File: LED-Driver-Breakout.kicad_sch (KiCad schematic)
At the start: 0 parts

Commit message: finished board - need review
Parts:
- added C1, C2: C, symbol Device:C
- added F1: Fuse, symbol Device:Fuse
- added PS1: LDH-45B-1050, LDH-45B-1050:CONV_LDH-45B-1050, symbol LDH-45B-1050:LDH-45B-1050
- added U1: V10P45-M3/86A, SOT_45-M3/86A_VIS, symbol 2026-02-02_22-16-14:V10P45-M3_86A
- added U2: TSR0.5-2418, Converter_DCDC:Converter_DCDC_TRACO_TSR0.5-24xx_TSR0.5-24xxx_THT, symbol Converter_DCDC:TSR0.5-2418
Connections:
- new net: F1.2, U1.1 (ANODE), U1.2 (ANODE)
- new net +BATT: F1.1
- new net GND: C1.2, C2.2, PS1.2 (VIN-), U2.2 (GND)
- new net VOUT+: PS1.7 (VOUT+)
- new net VOUT-: PS1.6 (VOUT-)
- new net VRegulated: U2.3 (Vout)
- new net V_Fused: C1.1, C2.1, PS1.1 (VIN+), U1.3 (CATHODE), U2.1 (Vin)

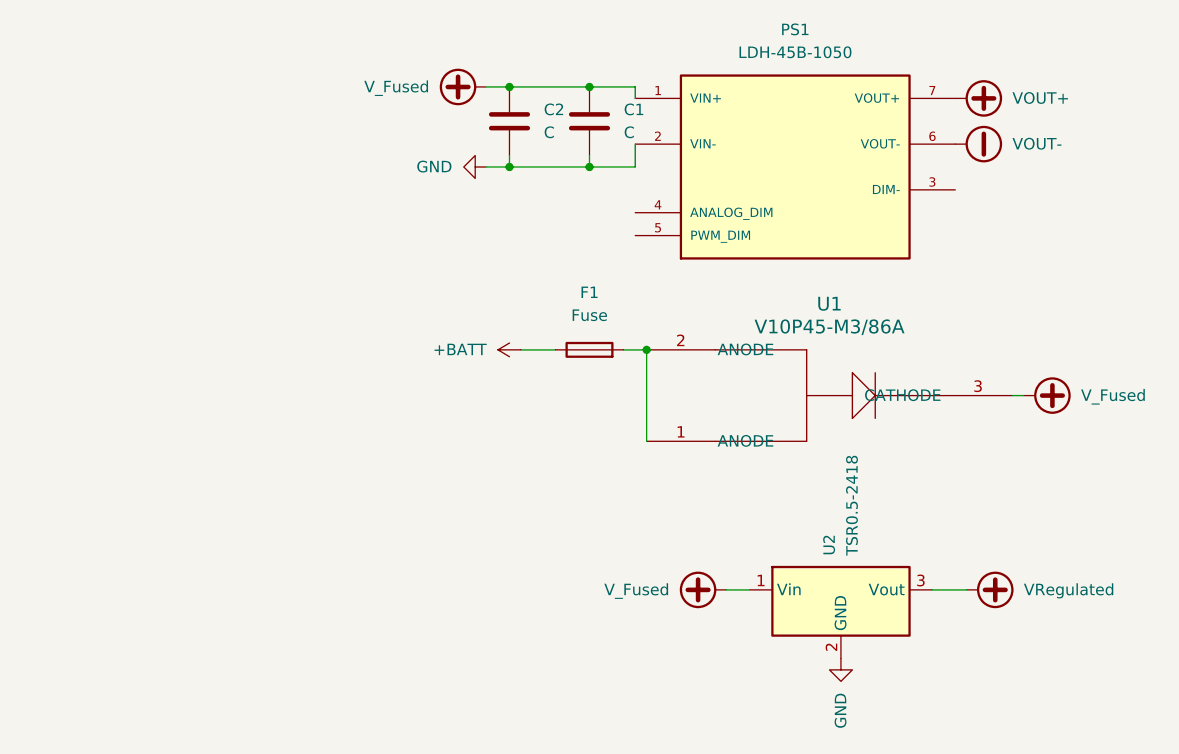
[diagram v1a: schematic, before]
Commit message: finished pcb routing may need to make the board more square
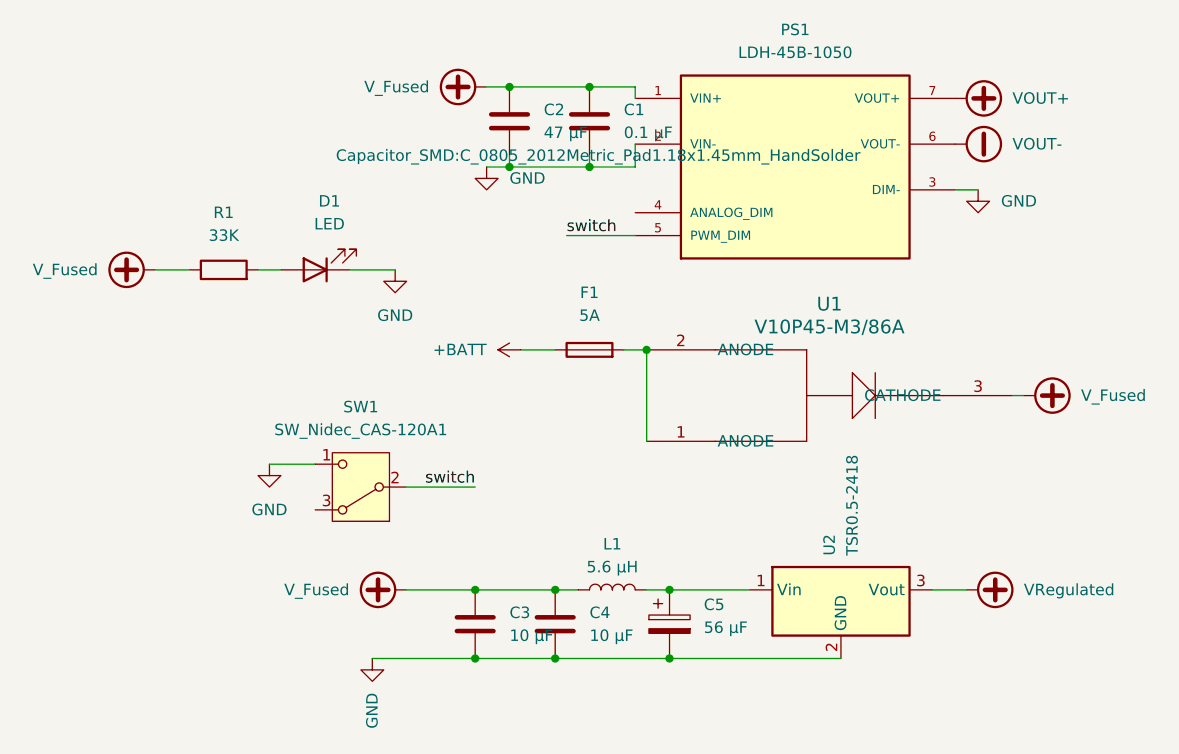
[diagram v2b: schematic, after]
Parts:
- added C3, C4: 10 µF, Capacitor_SMD:C_0805_2012Metric_Pad1.18x1.45mm_HandSolder, symbol Device:C
- added C5: 56 µF, Capacitor_SMD:CP_Elec_8x10, symbol Device:C_Polarized
- added D1: LED, LED_SMD:LED_1206_3216Metric_Pad1.42x1.75mm_HandSolder, symbol Device:LED
- added L1: 5.6 µH, Inductor_SMD:L_0805_2012Metric_Pad1.05x1.20mm_HandSolder, symbol Device:L
- added R1: 33K, Resistor_SMD:R_1206_3216Metric_Pad1.30x1.75mm_HandSolder, symbol Device:R
- added SW1: SW_Nidec_CAS-120A1, Button_Switch_SMD:Nidec_Copal_CAS-120A, symbol Switch:SW_Nidec_CAS-120A1
- C1: value C -> 0.1 µF; footprint (none) -> Capacitor_SMD:C_0805_2012Metric_Pad1.18x1.45mm_HandSolder
- C2: value C -> 47 µF; footprint (none) -> Capacitor_SMD:C_Elec_6.3x7.7
- F1: value Fuse -> 5A; footprint (none) -> KiCad333:154005DR
- PS1: footprint LDH-45B-1050:CONV_LDH-45B-1050 -> KiCad:LDH45B1050
- U1: footprint SOT_45-M3/86A_VIS -> Diode_SMD:D_PowerDI-5
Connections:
- net GND: now also PS1.3 (DIM-), C3.2, C4.2, C5.2, D1.1 (K), SW1.1 (C)
- net V_Fused: now also C3.1, C4.1, L1.1, R1.1; no longer U2.1 (Vin)
- net switch: now reaches PS1.5 (PWM_DIM)
- net switch: now also SW1.2 (B)
- new net: D1.2 (A), R1.2
- new net: C5.1, L1.2, U2.1 (Vin)

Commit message: Updates to schematic.
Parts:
- C1: footprint Capacitor_SMD:C_0805_2012Metric_Pad1.18x1.45mm_HandSolder -> C
- U2: value TSR0.5-2418 -> TSR0.5-24120
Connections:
- no-connect marks 0 -> 2
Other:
- note added: "12VDC Switching Regulator"
- note added: "LED On/Off Switch"
- note added: "Main LED Driver"
- note added: "Power Indicator"
- note added: "Reverse Polarity Protection"
- moved on the sheet: C1, C2, C3, C4, C5, D1, F1, L1, PS1, R1, SW1, U1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

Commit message: Added project-specific libs/fps; updates generally; broken rn.
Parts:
- removed F1: 5A, KiCad333:154005DR, symbol Device:Fuse
- removed PS1: LDH-45B-1050, KiCad:LDH45B1050, symbol LDH-45B-1050:LDH-45B-1050
- removed U1: V10P45-M3/86A, Diode_SMD:D_PowerDI-5, symbol 2026-02-02_22-16-14:V10P45-M3_86A
- removed U2: TSR0.5-24120, Converter_DCDC:Converter_DCDC_TRACO_TSR0.5-24xx_TSR0.5-24xxx_THT, symbol Converter_DCDC:TSR0.5-2418
- added C6: 10 µF, Capacitor_SMD:C_0805_2012Metric_Pad1.18x1.45mm_HandSolder, symbol Device:C
- added F1: 5A, Project_Footprints_Lib:154005DR, symbol Project_Symbols_Lib:Fuse
- added J1: S2B-XH-A, Project_Footprints_Lib:JST_XH_S2B-XH-A_1x02_P2.50mm_Horizontal, symbol Project_Symbols_Lib:Connector-JST-RAngle-2pin
- added J2: LED Output, TerminalBlock_WAGO:TerminalBlock_WAGO_2601-3102_1x02_P3.50mm_Vertical, symbol Project_Symbols_Lib:Connector-WAGO-clamp-4pos
- added PS1: LDH-45B-1050, Project_Footprints_Lib:LDH-45B-1050, symbol Project_Symbols_Lib:LDH-45B-1050
- added U1: V10P45-M3/86A, Diode_SMD:D_PowerDI-5, symbol Project_Symbols_Lib:V10P45-M3_86A
- added U2: TSR2-24120, Converter_DCDC:Converter_DCDC_TRACO_TSR2-xxxx_THT, symbol Converter_DCDC:TSR2-24120
- C1: footprint C -> Project_Footprints_Lib:C_0805_2012Metric_Pad1.18x1.45mm_HandSolder
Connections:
- net GND: now also PS1.3 (DIM-); no longer C1.2, C2.2, C3.2, C4.2, C5.2
- net V_Fused: now also PS1.1 (VIN+), U1.1
- net switch: now also PS1.5 (PWM_DIM)
- net at C5.1, L1.2: now also C6.1, U2.1 (Vin)
- new net: J2.1, PS1.7 (VOUT+)
- new net: J2.2, PS1.6 (VOUT-)
- new net: C3.2, C4.2, C5.2, C6.2, J1.2, U2.2 (GND)
- new net: C1.2, C2.2, PS1.2 (VIN-)
- new net: F1.2, U1.2
- new net: J1.1, U2.3 (Vout)
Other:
- note added: "* Create a GND net for KiCad ERC."
- moved on the sheet: C3, C4, C5, L1

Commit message: Relayout in progress.
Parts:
- removed SW1: SW_Nidec_CAS-120A1, Button_Switch_SMD:Nidec_Copal_CAS-120A, symbol Switch:SW_Nidec_CAS-120A1
- added J3: XT60, Connector_AMASS:AMASS_XT60PW-M_1x02_P7.20mm_Horizontal, symbol Project_Symbols_Lib:Connector-XT60M
- added J4: 01x03_PinHeaderSwitch, Connector_PinHeader_2.54mm:PinHeader_1x03_P2.54mm_Vertical, symbol Connector:Conn_01x03_Pin
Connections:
- net GND: now also J3.1, J4.1 (Pin_1)
- net switch: now also J4.2 (Pin_2)
- net at F1.1: now also J3.2
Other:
- note added: "Reverse Polarity Protection/Battery Input"
- note removed: "Reverse Polarity Protection"
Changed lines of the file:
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@@
 		)
 	)
-	(text "Reverse Polarity Protection"
-		(exclude_from_sim no)
-		(at 49.53 109.22 0)
+	(text "Reverse Polarity Protection/Battery Input"
+		(exclude_from_sim no)
+		(at 55.372 109.982 0)
 		(effects
 			(font
@@
 	)
 	(no_connect
-		(at 43.18 156.21)
+		(at 73.66 78.74)
 	)
 	(no_connect
-		(at 73.66 78.74)
+		(at 49.53 154.94)
+	)
+	(wire
+		(pts
+			(xy 50.8 129.54) (xy 52.07 129.54)
+		)
+		(stroke
+			(width 0)
+			(type default)
+		)
 	)
 	(wire
@@
 	(wire
 		(pts
-			(xy 38.1 151.13) (xy 43.18 151.13)
-		)
-		(stroke
-			(width 0)
-			(type default)
-		)
-	)
-	(wire
-		(pts
 			(xy 109.22 66.04) (xy 110.49 66.04)
 		)
@@
 	(wire
 		(pts
+			(xy 49.53 149.86) (xy 52.07 149.86)
+		)
+		(stroke
+			(width 0)
+			(type default)
+		)
+	)
+	(wire
+		(pts
 			(xy 46.99 175.26) (xy 48.26 175.26)
 		)
@@
 	(wire
 		(pts
-			(xy 60.96 153.67) (xy 53.34 153.67)
-		)
-		(stroke
-			(width 0)
-			(type default)
-		)
-	)
-	(wire
-		(pts
-			(xy 52.07 127) (xy 54.61 127)
-		)
-		(stroke
-			(width 0)
-			(type default)
-		)
-	)
-	(wire
-		(pts
 			(xy 109.22 71.12) (xy 110.49 71.12)
 		)
@@
 		(pts
 			(xy 118.11 177.8) (xy 118.11 182.88)
+		)
+		(stroke
+			(width 0)
+			(type default)
+		)
+	)
+	(wire
+		(pts
+			(xy 49.53 152.4) (xy 52.07 152.4)
+		)
+		(stroke
+			(width 0)
+			(type default)
+		)
+	)
+	(wire
+		(pts
+			(xy 50.8 127) (xy 54.61 127)
 		)
 		(stroke
@@
 	)
 	(label "GND"
+		(at 52.07 129.54 0)
+		(effects
+			(font
+				(size 1.27 1.27)
+			)
+			(justify left bottom)
+		)
+	)
+	(label "GND"
 		(at 111.76 76.2 0)
 		(effects
@@
 	)
 	(label "GND"
-		(at 38.1 151.13 180)
+		(at 52.07 149.86 0)
 		(effects
 			(font
 				(size 1.27 1.27)
 			)
-			(justify right bottom)
+			(justify left bottom)
 		)
 	)
@@
 	)
 	(label "switch"
-		(at 60.96 153.67 180)
+		(at 52.07 152.4 0)
 		(effects
 			(font
 				(size 1.27 1.27)
 			)
-			(justify right bottom)
+			(justify left bottom)
 		)
 	)
@@
 	)
 	(symbol
-		(lib_id "Switch:SW_Nidec_CAS-120A1")
-		(at 48.26 153.67 180)
-		(unit 1)
-		(exclude_from_sim no)
-		(in_bom yes)
-		(on_board no)
-		(dnp no)
-		(fields_autoplaced yes)
-		(property "Reference" "SW1"
-			(at 48.26 144.78 0)
-			(effects
-				(font
-					(size 1.27 1.27)
-				)
-			)
-		)
-		(property "Value" "SW_Nidec_CAS-120A1"
-			(at 48.26 147.32 0)
-			(effects
-				(font
-					(size 1.27 1.27)
-				)
-			)
-		)
-		(property "Footprint" "Button_Switch_SMD:Nidec_Copal_CAS-120A"
-			(at 48.26 143.51 0)
-			(effects
-				(font
-					(size 1.27 1.27)
-				)
-				(hide yes)
-			)
-		)
-		(property "Datasheet" "https://www.nidec-components.com/e/catalog/switch/cas.pdf"
-			(at 48.26 146.05 0)
-			(effects
-				(font
-					(size 1.27 1.27)
-				)
-				(hide yes)
-			)
-		)
-		(property "Description" "Switch, single pole double throw"
-			(at 48.26 153.67 0)
-			(effects
-				(font
-					(size 1.27 1.27)
-				)
-				(hide yes)
-			)
-		)
-		(pin "1"
-		)
-		(pin "3"
-		)
-		(pin "2"
-		)
-		(instances
-			(project ""
-				(path "/489043bf-45bc-433c-85b5-ac7612966c0c"
-					(reference "SW1")
-					(unit 1)
-				)
-			)
-		)
-	)
-	(symbol
 		(lib_id "Device:C")
 		(at 48.26 179.07 0)
@@
 	)
 	(symbol
+		(lib_id "Connector:Conn_01x03_Pin")
+		(at 44.45 152.4 0)
+		(unit 1)
+		(exclude_from_sim no)
+		(in_bom yes)
+		(on_board yes)
+		(dnp no)
+		(property "Reference" "J4"
+			(at 44.958 146.05 0)
+			(effects
+				(font
+					(size 1.27 1.27)
+				)
+			)
+		)
+		(property "Value" "01x03_PinHeaderSwitch"
+			(at 45.085 147.32 0)
+			(effects
+				(font
+					(size 1.27 1.27)
+				)
+				(hide yes)
+			)
+		)
+		(property "Footprint" "Connector_PinHeader_2.54mm:PinHeader_1x03_P2.54mm_Vertical"
+			(at 44.45 152.4 0)
+			(effects
+				(font
+					(size 1.27 1.27)
+				)
+				(hide yes)
+			)
+		)
+		(property "Datasheet" "~"
+			(at 44.45 152.4 0)
+			(effects
+				(font
+					(size 1.27 1.27)
+				)
+				(hide yes)
+			)
+		)
+		(property "Description" "Generic connector, single row, 01x03, script generated"
+			(at 44.45 152.4 0)
+			(effects
+				(font
+					(size 1.27 1.27)
+				)
+				(hide yes)
+			)
+		)
+		(pin "3"
+		)
+		(pin "1"
+		)
+		(pin "2"
+		)
+		(instances
+			(project ""
+				(path "/489043bf-45bc-433c-85b5-ac7612966c0c"
+					(reference "J4")
+					(unit 1)
+				)
+			)
+		)
+	)
+	(symbol
 		(lib_id "Project_Symbols_Lib:LDH-45B-1050")
 		(at 91.44 73.66 0)
@@
 	)
 	(symbol
-		(lib_id "power:+BATT")
-		(at 52.07 127 90)
-		(unit 1)
-		(exclude_from_sim no)
-		(in_bom yes)
-		(on_board yes)
-		(dnp no)
-		(fields_autoplaced yes)
-		(property "Reference" "#PWR07"
-			(at 55.88 127 0)
-			(effects
-				(font
-					(size 1.27 1.27)
-				)
-				(hide yes)
-			)
-		)
-		(property "Value" "+BATT"
-			(at 48.26 126.9999 90)
-			(effects
-				(font
-					(size 1.27 1.27)
-				)
-				(justify left)
-			)
-		)
-		(property "Footprint" ""
-			(at 52.07 127 0)
-			(effects
-				(font
-					(size 1.27 1.27)
-				)
-				(hide yes)
-			)
-		)
-		(property "Datasheet" ""
-			(at 52.07 127 0)
-			(effects
-				(font
-					(size 1.27 1.27)
-				)
-				(hide yes)
-			)
-		)
-		(property "Description" "Power symbol creates a global label with name \"+BATT\""
-			(at 52.07 127 0)
-			(effects
-				(font
-					(size 1.27 1.27)
-				)
-				(hide yes)
-			)
-		)
-		(pin "1"
-		)
-		(instances
-			(project ""
-				(path "/489043bf-45bc-433c-85b5-ac7612966c0c"
-					(reference "#PWR07")
-					(unit 1)
-				)
-			)
-		)
-	)
-	(symbol
 		(lib_id "Device:C_Polarized")
 		(at 87.63 179.07 0)
@@
 					(unit 1)
 				)
+			)
+		)
+	)
+	(symbol
+		(lib_id "Project_Symbols_Lib:Connector-XT60M")
+		(at 48.26 128.27 180)
+		(unit 1)
+		(exclude_from_sim no)
+		(in_bom yes)
+		(on_board yes)
+		(dnp no)
+		(fields_autoplaced yes)
+		(property "Reference" "J3"
+			(at 46.99 120.65 0)
+			(effects
+				(font
+					(size 1.27 1.27)
+				)
+			)
+		)
+		(property "Value" "XT60"
+			(at 46.99 123.19 0)
+			(effects
+				(font
+					(size 1.27 1.27)
+				)
+			)
+		)
+		(property "Footprint" "Connector_AMASS:AMASS_XT60PW-M_1x02_P7.20mm_Horizontal"
+			(at 48.26 128.27 0)
+			(effects
+				(font
+					(size 1.27 1.27)
+				)
+				(hide yes)
+			)
+		)
+		(property "Datasheet" "https://www.tme.com/Document/b13629717d44ae038681dba08d18c0b6/XT60PW-M.pdf"
+			(at 48.26 128.27 0)
+			(effects
+				(font
+					(size 1.27 1.27)
+				)
+				(hide yes)
+			)
+		)
+		(property "Description" "JST, 2-pin THT connector."
+			(at 48.26 128.27 0)
+			(effects
+				(font
+					(size 1.27 1.27)
+				)
+				(hide yes)
+			)
+		)
+		(pin "2"
+		)
+		(pin "1"
+		)
+		(instances
+			(project ""
+				(path "/489043bf-45bc-433c-85b5-ac7612966c0c"
+					(reference "J3")
+					(unit 1)
+				)

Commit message: did layout, still need to fix ERC errors and DRC warnings
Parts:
- added DRIVER_V_IN1, GND1, REGULATOR_IN1, SWITCH1, V_FUSED1, V_REGULATED1: TestPoint, TestPoint:TestPoint_Loop_D2.54mm_Drill1.5mm_Beaded, symbol Connector:TestPoint
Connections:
- net REGULATOR_V_IN: now reaches C5.1, C6.1, L1.2, U2.1 (Vin)
- net REGULATOR_V_IN: now also REGULATOR_IN1.1
- net V_REGULATED: now reaches J1.1, U2.3 (Vout)
- net V_REGULATED: now also V_REGULATED1.1
- removed net GND: D1.1 (K), J3.1, J4.1 (Pin_1), PS1.3 (DIM-)
- net V_Fused renamed +24V
- net +24V: now also DRIVER_V_IN1.1, V_FUSED1.1
- net switch renamed SWITCH
- net SWITCH: now also SWITCH1.1
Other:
- note added: "Test Points"
- note removed: "* Create a GND net for KiCad ERC."
- moved on the sheet: C1, C2, C3, C4, C5, C6, D1, F1, J1, J2, J4, L1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

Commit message: Tiny updates.
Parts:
- removed DRIVER_V_IN1: TestPoint, TestPoint:TestPoint_Loop_D2.54mm_Drill1.5mm_Beaded, symbol Connector:TestPoint
- removed U2: TSR2-24120, Converter_DCDC:Converter_DCDC_TRACO_TSR2-xxxx_THT, symbol Converter_DCDC:TSR2-24120
- added U3: TSR2-24120, Converter_DCDC:Converter_DCDC_TRACO_TSR2-xxxx_THT, symbol Project_Symbols_Lib:TSR2-24120
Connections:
- net REGULATOR_V_IN: now also U3.1 (Vin)
- net V_REGULATED: now also U3.3 (Vout)
- net GND: now reaches C3.2, C4.2, C5.2, C6.2, J1.2
- net GND: now also C1.2, C2.2, D1.1 (K), GND1.1, J3.1, J4.1 (Pin_1), PS1.2 (VIN-), U3.2 (GND)
- no-connect marks 2 -> 3
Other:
- note added: "KiCad hack for passing ERC."
- moved on the sheet: J3, REGULATOR_IN1, SWITCH1, V_FUSED1, V_REGULATED1
